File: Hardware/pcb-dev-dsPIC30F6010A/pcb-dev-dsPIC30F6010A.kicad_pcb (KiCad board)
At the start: 2 copper layers, 32 parts, among them J1 Left Berg Strip, J2 PICkit connector, J3 Right Berg Strip, U1 DSPIC30F6010A-30I_PF, Y1 10MHz

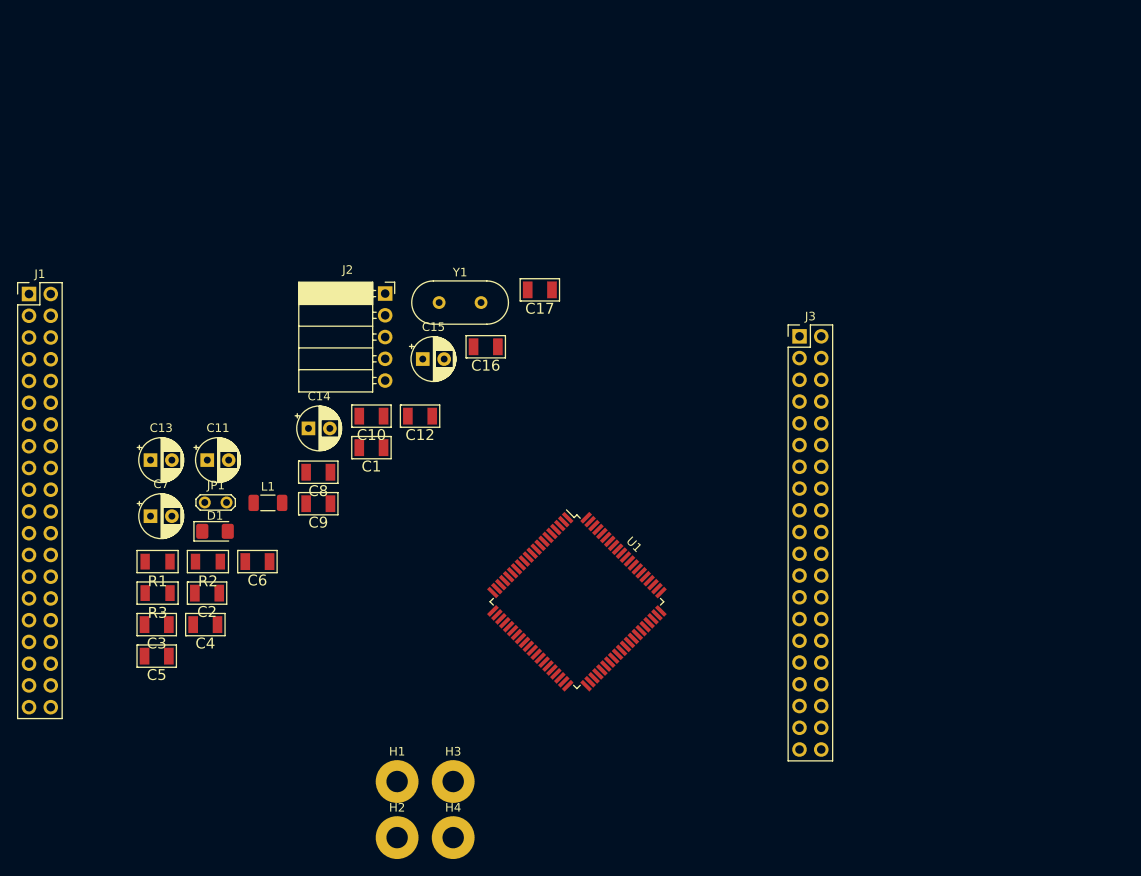
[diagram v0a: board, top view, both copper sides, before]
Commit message: Add edge cuts and power planes. Work in progress
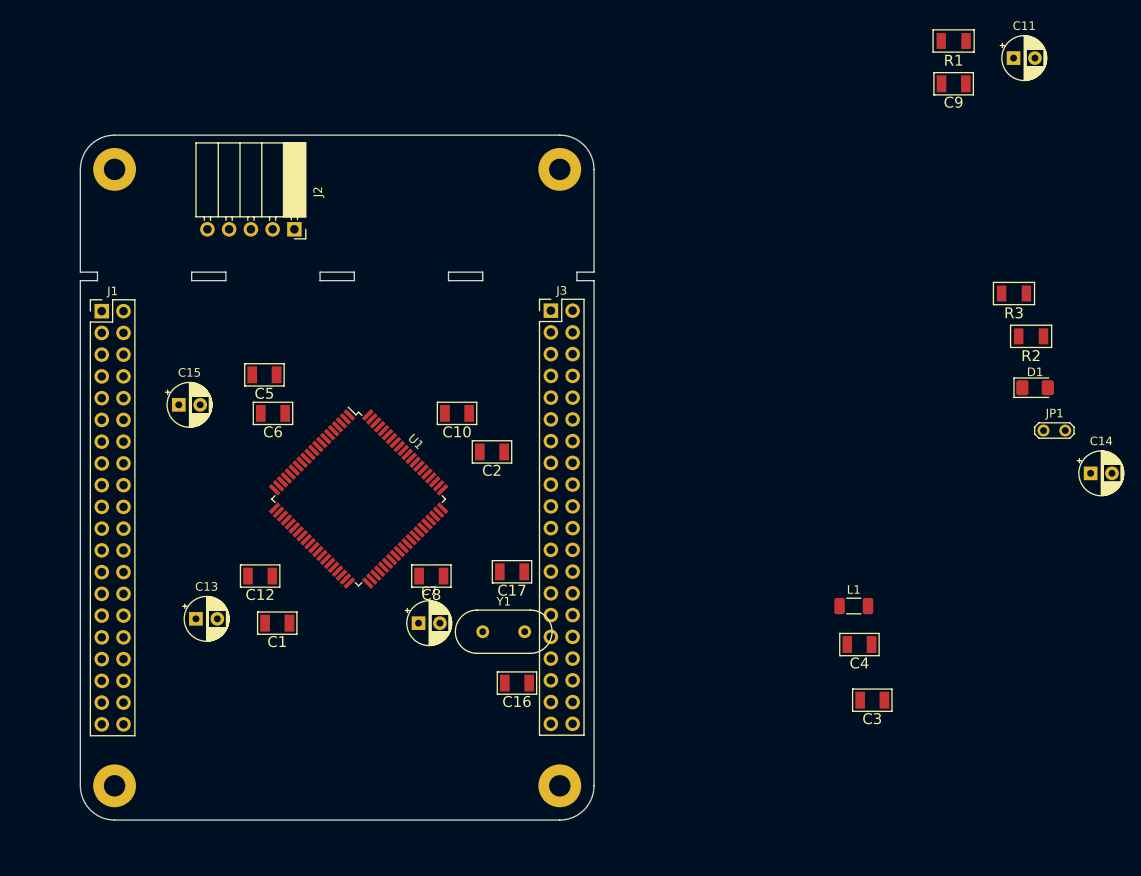
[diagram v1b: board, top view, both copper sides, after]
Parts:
- moved R1 111.1 mm to (235.0, 49.0)
- moved R3 106.0 mm to (242.1, 78.5)
- moved C11 105.2 mm to (242.0, 51.0)
- moved R2 99.7 mm to (244.1, 83.5)
- moved JP1 98.3 mm to (245.5, 94.5)
- moved D1 97.2 mm to (244.5, 89.5)
- moved C14 91.5 mm to (251.0, 99.5)
- moved C9 89.0 mm to (235.0, 54.0)
- moved C3 84.0 mm to (225.5, 126.0)
- moved H1 78.7 mm to (137.0, 64.0)
- moved C4 76.4 mm to (224.0, 119.5)
- moved H3 72.6 mm to (189.0, 64.0)
- moved L1 69.5 mm to (223.3, 115.0)
- moved C16 39.4 mm to (184.0, 124.0)
- moved Y1 38.8 mm to (180.0, 118.0)
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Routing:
- added copper zone on In1.Cu, net +5V
- added copper zone on In2.Cu, net GND
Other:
- board outline added: 60 x 80 mm
- copper layers 2 -> 4

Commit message: Routed a few decoupling capacitors and pins. Work in progress
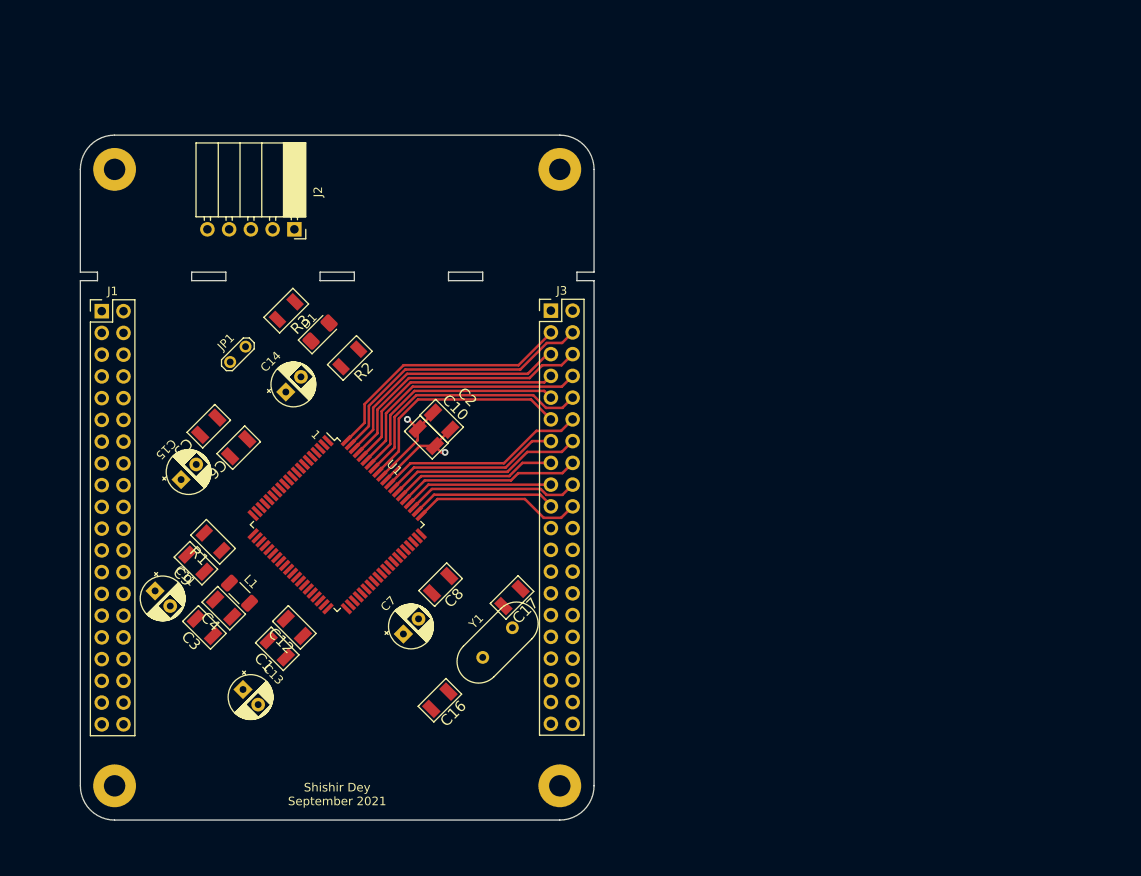
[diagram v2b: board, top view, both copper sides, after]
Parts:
- moved C11 118.0 mm to (141.7, 113.2), turned to 315 degrees
- moved C9 104.7 mm to (146.5, 110.0), turned to 315 degrees
- moved R1 104.4 mm to (148.5, 107.5), turned to 315 degrees
- moved JP1 95.3 mm to (150.5, 86.5), turned to 45 degrees
- moved C14 94.5 mm to (157.0, 90.0), turned to 45 degrees
- moved R3 85.0 mm to (157.1, 80.5), turned to 45 degrees
- moved D1 83.8 mm to (161.0, 83.0), turned to 45 degrees
- moved R2 79.6 mm to (164.5, 86.0), turned to 45 degrees
- moved C3 78.5 mm to (147.5, 117.5), turned to 315 degrees
- moved C4 74.4 mm to (149.8, 115.2), turned to 315 degrees
- moved L1 71.8 mm to (151.6, 113.5), turned to 315 degrees
- moved C13 9.92 mm to (152.0, 124.8), turned to 315 degrees
- moved C16 9.22 mm to (175.0, 126.0), turned to 45 degrees
- moved C5 8.85 mm to (148.0, 94.0), turned to 225 degrees
- moved C15 8.74 mm to (144.8, 100.2), turned to 45 degrees
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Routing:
- net RE3: track 0.00 -> 32.8 mm
- net RE1: track 0.00 -> 31.4 mm
- net RE4: track 0.00 -> 30.4 mm
- net RG0: track 0.00 -> 30.1 mm
- net RF1: track 0.00 -> 30.0 mm
- net RE2: track 0.00 -> 29.0 mm
- net RE0: track 0.00 -> 27.7 mm
- net RG1: track 0.00 -> 27.0 mm
- net RF0: track 0.00 -> 26.9 mm
- net RD7: track 0.00 -> 24.5 mm
- net RD5: track 0.00 -> 22.9 mm
- net RD13: track 0.00 -> 21.3 mm
- net RD6: track 0.00 -> 20.6 mm
- net RD3: track 0.00 -> 20.3 mm
- net RD1: track 0.00 -> 20.0 mm
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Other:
- board text added: "1"
- board text added: "Shishir Dey September 2021"

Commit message: Routed a few decoupling capacitors and pins. Added PCB images. Work in progress
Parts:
- moved C17 16.7 mm to (173.0, 127.0), turned to 315 degrees
- moved C16 12.8 mm to (183.5, 116.5), turned to 315 degrees
- moved C8 4.77 mm to (173.5, 117.0)
- moved C7 1.75 mm to (170.5, 120.0), turned to 225 degrees
- moved Y1 1.00 mm to (180.0, 120.0), turned to 225 degrees
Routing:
- net RF8: track 0.00 -> 45.3 mm
- net RF6: track 0.00 -> 45.3 mm
- net RG2: track 0.00 -> 45.0 mm
- net RF3: track 0.00 -> 44.4 mm
- net RF7: track 0.00 -> 42.2 mm
- net RG3: track 0.00 -> 42.2 mm
- net RF2: track 0.00 -> 41.6 mm
- net RA15: track 0.00 -> 23.4 mm
- net RD9: track 0.00 -> 21.9 mm
- net RD11: track 0.00 -> 21.3 mm
- net RC13: track 0.00 -> 21.3 mm
- net RA14: track 0.00 -> 21.2 mm
- net Net-(C17-Pad2): track 0.00 -> 21.1 mm
- net Net-(C16-Pad1): track 0.00 -> 21.0 mm
- net RD8: track 0.00 -> 19.6 mm
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
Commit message: Routed a few pins. Work in progress
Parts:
- moved C14 46.6 mm to (202.2, 78.8)
- moved D1 46.6 mm to (206.2, 71.8)
- moved JP1 46.6 mm to (195.8, 75.2)
- moved R2 46.6 mm to (209.7, 74.8)
- moved R3 46.6 mm to (202.3, 69.2)
- moved C6 5.37 mm to (149.0, 91.7), turned to 45 degrees
- moved C15 3.38 mm to (146.8, 97.5), turned to 135 degrees
- moved C5 3.01 mm to (151.0, 93.7), turned to 45 degrees
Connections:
- J1 pad 15: RE9 -> RB5
- J1 pad 16: RB5 -> RE9
- J1 pad 17: RB4 -> RB3
- J1 pad 18: RB3 -> RB4
- J1 pad 19: RB2 -> RB6
- J1 pad 20: RB6 -> RB2
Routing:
- net RE5: track 0.00 -> 32.6 mm
- net RE7: track 0.00 -> 32.0 mm
- net RC3: track 0.00 -> 32.0 mm
- net RG9: track 0.00 -> 32.0 mm
- net RG7: track 0.00 -> 31.9 mm
- net RE6: track 0.00 -> 29.0 mm
- net RC1: track 0.00 -> 28.9 mm
- net RG6: track 0.00 -> 28.9 mm
- net RG8: track 0.00 -> 28.7 mm
- net RB5: track 0.00 -> 21.6 mm
- net RE8: track 0.00 -> 20.6 mm
- net RB3: track 0.00 -> 20.6 mm
- net RE9: track 0.00 -> 19.4 mm
- net RB4: track 0.00 -> 17.7 mm
- net RB2: track 0.00 -> 16.8 mm
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
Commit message: Routed a few pins. Add images. Work in progress
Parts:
- moved C12 5.30 mm to (152.8, 118.3), turned to 135 degrees
- moved C1 3.95 mm to (154.8, 116.3), turned to 135 degrees
- moved C13 2.89 mm to (150.5, 122.3), turned to 135 degrees
- moved C3 1.27 mm to (147.2, 116.2)
- moved C4 1.27 mm to (149.5, 114.0)
- moved L1 1.27 mm to (151.3, 112.2)
- moved R1 1.25 mm to (147.8, 108.5), turned to 135 degrees
- moved C9 0.90 mm to (145.7, 110.5)
- moved C11 0.73 mm to (141.8, 112.5)
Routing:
- net RF5: track 0.00 -> 36.4 mm
- net RD15: track 0.00 -> 36.3 mm
- net RB15: track 0.00 -> 36.1 mm
- net RB13: track 0.00 -> 36.1 mm
- net RF4: track 0.00 -> 33.3 mm
- net RD14: track 0.00 -> 33.1 mm
- net RB14: track 0.00 -> 33.0 mm
- net RB12: track 0.00 -> 33.0 mm
- net +5V: track 42.2 -> 71.2 mm, vias 2 -> 4
- net GND: track 38.3 -> 64.9 mm, vias 4 -> 5
- net RB7: track 0.00 -> 20.3 mm
- net RB6: track 0.00 -> 19.0 mm
- net VSSA: track 0.00 -> 18.3 mm
- net VREF+: track 0.00 -> 15.6 mm

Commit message: Routine done. Add images
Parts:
- moved R2 46.2 mm to (164.6, 65.0), turned to 180 degrees
- moved D1 36.9 mm to (170.0, 65.0), turned to 180 degrees
- moved R3 36.8 mm to (165.5, 69.5), turned to 270 degrees
- moved JP1 33.9 mm to (162.5, 68.5), turned to 270 degrees
- moved C14 33.3 mm to (170.0, 70.5), turned to 90 degrees
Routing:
- net PGD: track 0.00 -> 51.3 mm, vias 0 -> 1
- net PGC: track 0.00 -> 44.5 mm, vias 0 -> 1
- net MCLR: track 0.00 -> 37.8 mm, vias 0 -> 1
- net Net-(C14-Pad1): track 0.00 -> 14.7 mm
- net +5V: track 71.2 -> 77.5 mm, vias 4 -> 7
- net Net-(JP1-Pad1): track 0.00 -> 3.21 mm
- net VSSA: track 18.3 -> 17.7 mm

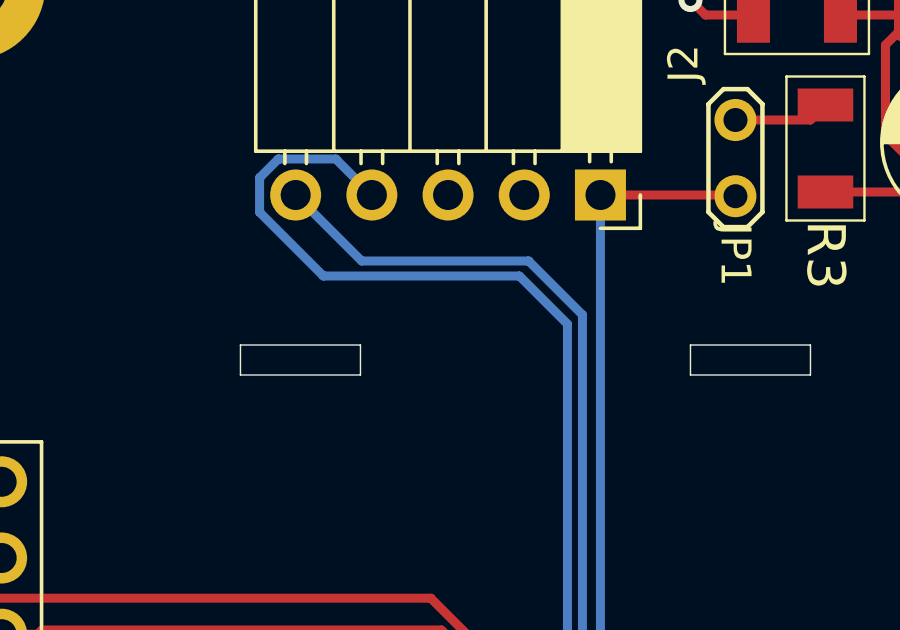
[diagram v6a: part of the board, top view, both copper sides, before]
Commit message: Add labels on the PICkit connector
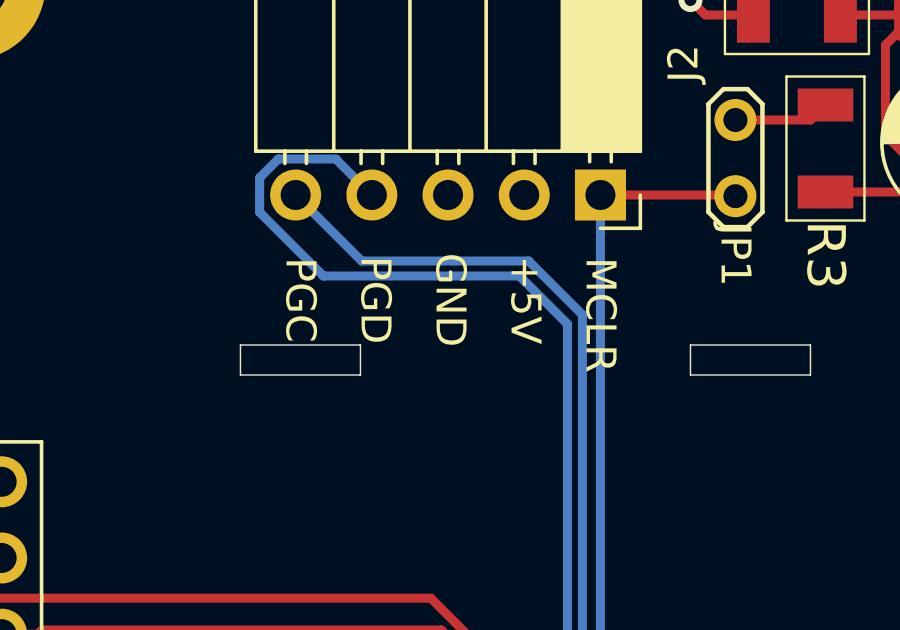
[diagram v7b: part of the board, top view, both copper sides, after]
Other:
- board text added: "+5V"
- board text added: "GND"
- board text added: "MCLR"
- board text added: "PGC"
- board text added: "PGD"
